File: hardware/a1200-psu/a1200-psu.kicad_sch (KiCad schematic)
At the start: 57 parts, among them J1 220V, J2 Conn_01x05, Q1 BC327, Q2 BC327, Q3 BU508AF, SW1 SW_SPST, U1 CNY17-2, U2 TL431D

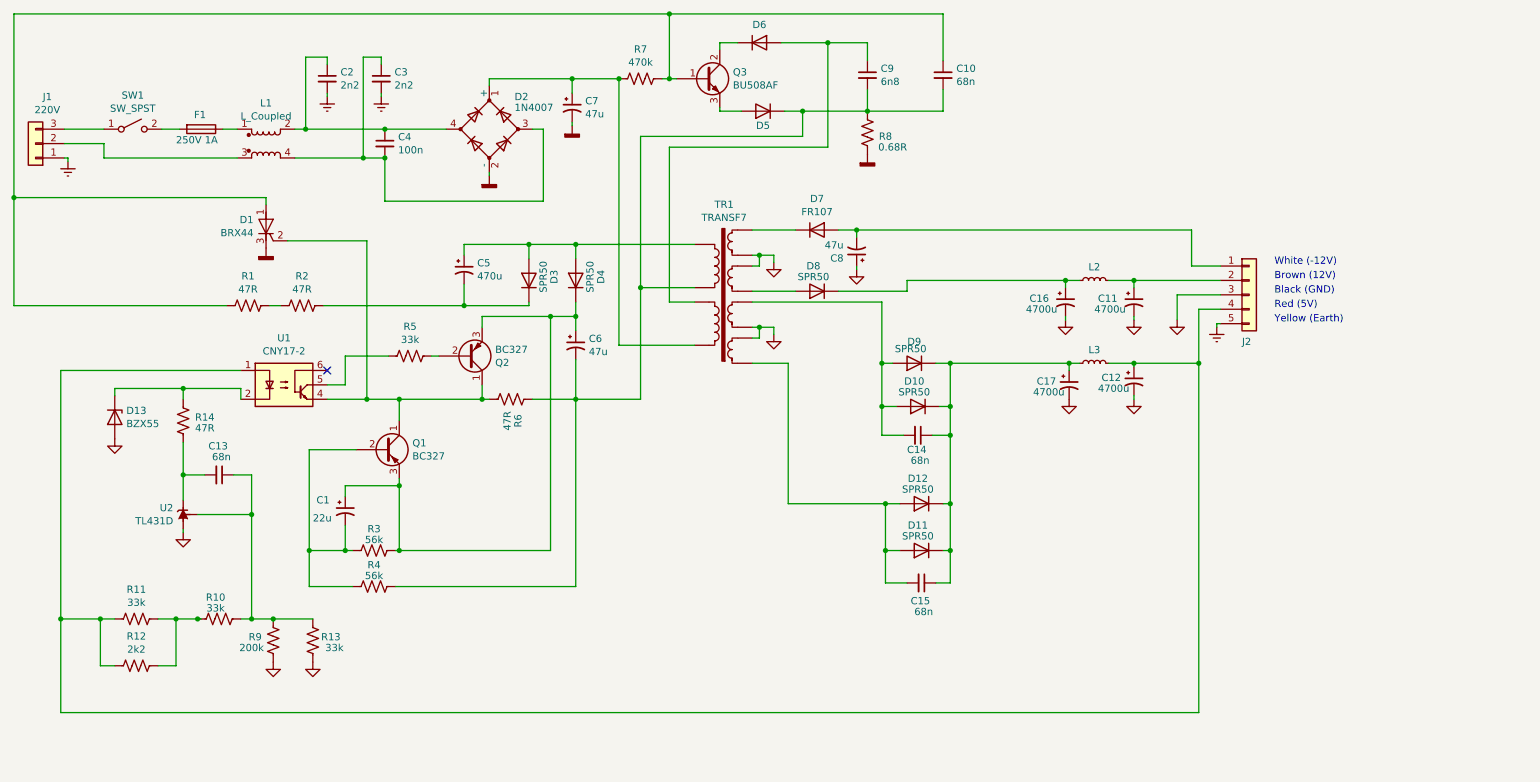
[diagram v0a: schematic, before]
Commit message: Add NTC and LF caps
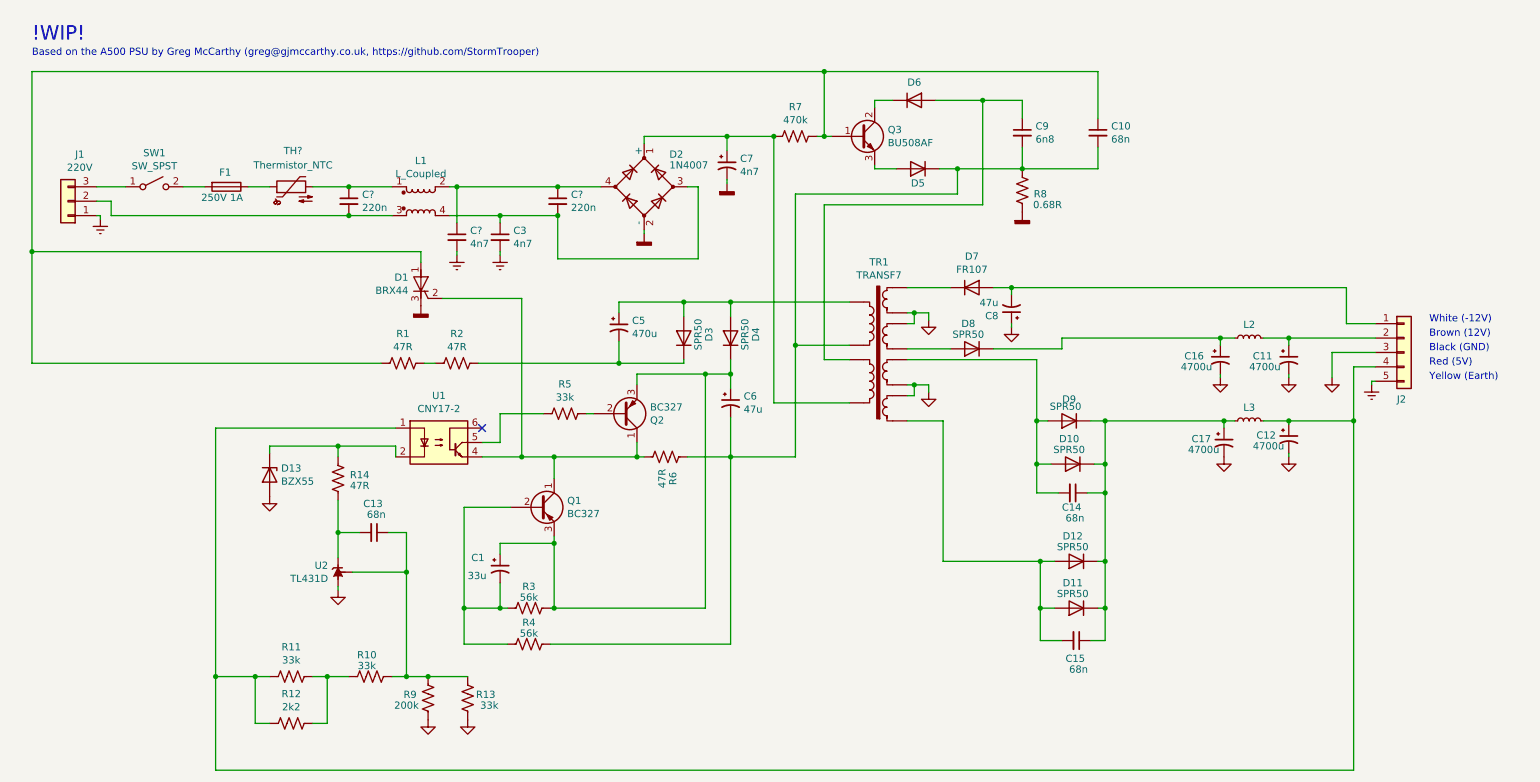
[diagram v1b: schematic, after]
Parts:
- removed C2: 2n2, symbol Device:C_Small
- removed C4: 100n, symbol Device:C_Small
- added C?: 4n7, symbol Device:C_Small
- added C? (x2): 220n, symbol Device:C_Small
- added TH?: Thermistor_NTC, symbol Device:Thermistor_NTC
- C1: value 22u -> 33u
- C3: value 2n2 -> 4n7
- C7: value 47u -> 4n7
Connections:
- net Earth: now also C?.2
- net at F1.1: now also TH?.1; no longer L1.1
- net at D2.4, L1.2: now also C?.1, C?.1
- net at J1.2 (Pin_2), L1.3: now also C?.2
- net at C3.1, D2.3, L1.4: now also C?.2
- new net: C?.1, L1.1, TH?.2
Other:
- note added: "!WIP!"
- note added: "Based on the A500 PSU by Greg McCarthy (greg@gjmccarthy.co.uk, https://github.com/StormTrooper)"
- company: (none) -> Nick Bolton
- title: Commodore A500 Power Supply  312503-03 -> Commodore A1200 Power Supply  391029-02
- moved on the sheet: C1, C10, C11, C12, C13, C14, C15, C16, C17, C3, C5, C6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

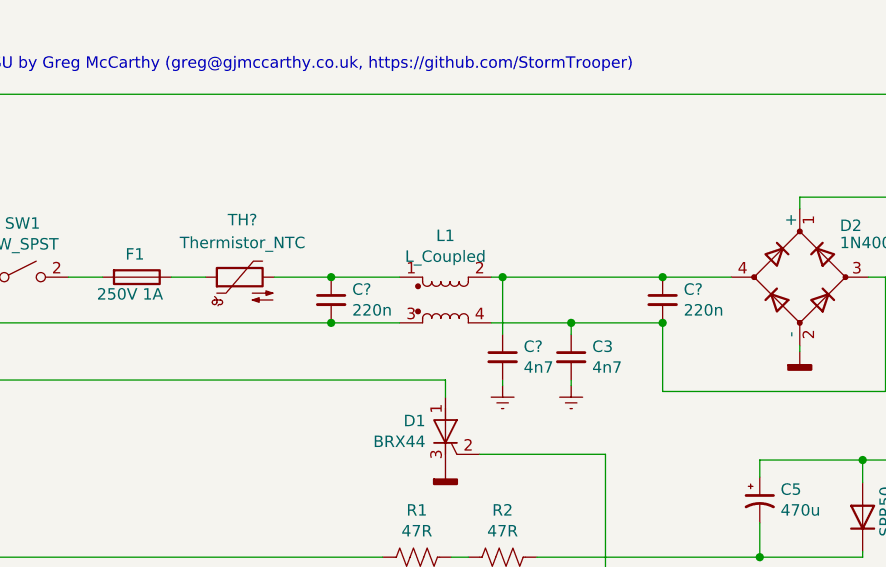
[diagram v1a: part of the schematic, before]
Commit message: Set TH value and annotate
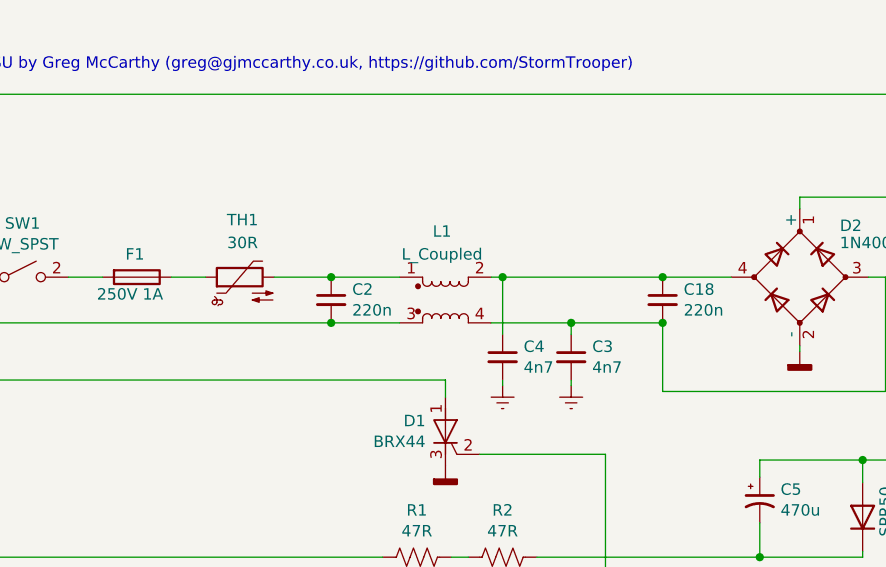
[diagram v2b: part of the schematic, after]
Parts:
- TH1: renamed from TH?; value Thermistor_NTC -> 30R
- gave numbers to parts that had none: 3
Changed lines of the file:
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@@
   )
   (symbol (lib_id "Device:L_Coupled") (at 87.63 46.99 0) (unit 1)
-    (in_bom yes) (on_board yes)
-    (property "Reference" "L1" (id 0) (at 87.63 39.8526 0))
-    (property "Value" "L_Coupled" (id 1) (at 87.63 42.164 0))
+    (in_bom yes) (on_board yes) (fields_autoplaced)
+    (property "Reference" "L1" (id 0) (at 87.249 39.37 0))
+    (property "Value" "L_Coupled" (id 1) (at 87.249 41.91 0))
     (property "Footprint" "" (id 2) (at 87.63 46.99 0)
       (effects (font (size 1.27 1.27)) hide)
@@
   (symbol (lib_id "Device:C_Small") (at 93.98 53.34 0) (unit 1)
     (in_bom yes) (on_board yes)
-    (property "Reference" "C?" (id 0) (at 96.3168 52.1716 0)
+    (property "Reference" "C4" (id 0) (at 96.3168 52.1716 0)
       (effects (font (size 1.27 1.27)) (justify left))
     )
@@
   (symbol (lib_id "power:Earth") (at 93.98 56.515 0) (unit 1)
     (in_bom yes) (on_board yes)
-    (property "Reference" "#PWR?" (id 0) (at 93.98 62.865 0)
+    (property "Reference" "#PWR03" (id 0) (at 93.98 62.865 0)
       (effects (font (size 1.27 1.27)) hide)
     )
@@
   (symbol (lib_id "Device:Thermistor_NTC") (at 64.77 44.45 90) (unit 1)
     (in_bom yes) (on_board yes) (fields_autoplaced)
-    (property "Reference" "TH?" (id 0) (at 65.0875 38.1 90))
-    (property "Value" "Thermistor_NTC" (id 1) (at 65.0875 40.64 90))
+    (property "Reference" "TH1" (id 0) (at 65.0875 38.1 90))
+    (property "Value" "30R" (id 1) (at 65.0875 40.64 90))
     (property "Footprint" "" (id 2) (at 63.5 44.45 0)
       (effects (font (size 1.27 1.27)) hide)
@@
   (symbol (lib_id "Device:C_Small") (at 111.76 46.99 0) (unit 1)
     (in_bom yes) (on_board yes)
-    (property "Reference" "C?" (id 0) (at 114.0968 45.8216 0)
+    (property "Reference" "C18" (id 0) (at 114.0968 45.8216 0)
       (effects (font (size 1.27 1.27)) (justify left))
     )
@@
   (symbol (lib_id "Device:C_Small") (at 74.93 46.99 0) (unit 1)
     (in_bom yes) (on_board yes)
-    (property "Reference" "C?" (id 0) (at 77.2668 45.8216 0)
+    (property "Reference" "C2" (id 0) (at 77.2668 45.8216 0)
       (effects (font (size 1.27 1.27)) (justify left))
     )
@@
       (reference "#PWR02") (unit 1) (value "GNDD") (footprint "")
     )
+    (path "/140d05a2-eaad-4824-bf22-b4c1b5fc3c05"
+      (reference "#PWR03") (unit 1) (value "Earth") (footprint "")
+    )
     (path "/00000000-0000-0000-0000-00005e6bda05"
       (reference "#PWR04") (unit 1) (value "Earth") (footprint "")
@@
       (reference "#PWR020") (unit 1) (value "GND") (footprint "")
     )
-    (path "/140d05a2-eaad-4824-bf22-b4c1b5fc3c05"
-      (reference "#PWR?") (unit 1) (value "Earth") (footprint "")
-    )
     (path "/00000000-0000-0000-0000-00005e80fecf"
       (reference "C1") (unit 1) (value "33u") (footprint "")
     )
+    (path "/9bd3b76d-6431-4e72-98c0-8c8f9369d359"
+      (reference "C2") (unit 1) (value "220n") (footprint "")
+    )
     (path "/00000000-0000-0000-0000-00005e6976c3"
       (reference "C3") (unit 1) (value "4n7") (footprint "")
     )
+    (path "/0e475606-0972-410d-9d2a-e185de5dfec3"
+      (reference "C4") (unit 1) (value "4n7") (footprint "")
+    )
     (path "/00000000-0000-0000-0000-00005e74c909"
       (reference "C5") (unit 1) (value "470u") (footprint "")
@@
       (reference "C17") (unit 1) (value "4700u") (footprint "")
     )
-    (path "/0e475606-0972-410d-9d2a-e185de5dfec3"
-      (reference "C?") (unit 1) (value "4n7") (footprint "")
-    )
     (path "/57508837-9844-4605-9233-1414d37064cf"
-      (reference "C?") (unit 1) (value "220n") (footprint "")
-    )
-    (path "/9bd3b76d-6431-4e72-98c0-8c8f9369d359"
-      (reference "C?") (unit 1) (value "220n") (footprint "")
+      (reference "C18") (unit 1) (value "220n") (footprint "")
     )
     (path "/00000000-0000-0000-0000-00005e6b8e8b"
@@
     )
     (path "/2facb6fc-ac96-441e-9800-d8af24285397"
-      (reference "TH?") (unit 1) (value "Thermistor_NTC") (footprint "")
+      (reference "TH1") (unit 1) (value "30R") (footprint "")
     )
     (path "/00000000-0000-0000-0000-00005e6e99dc"

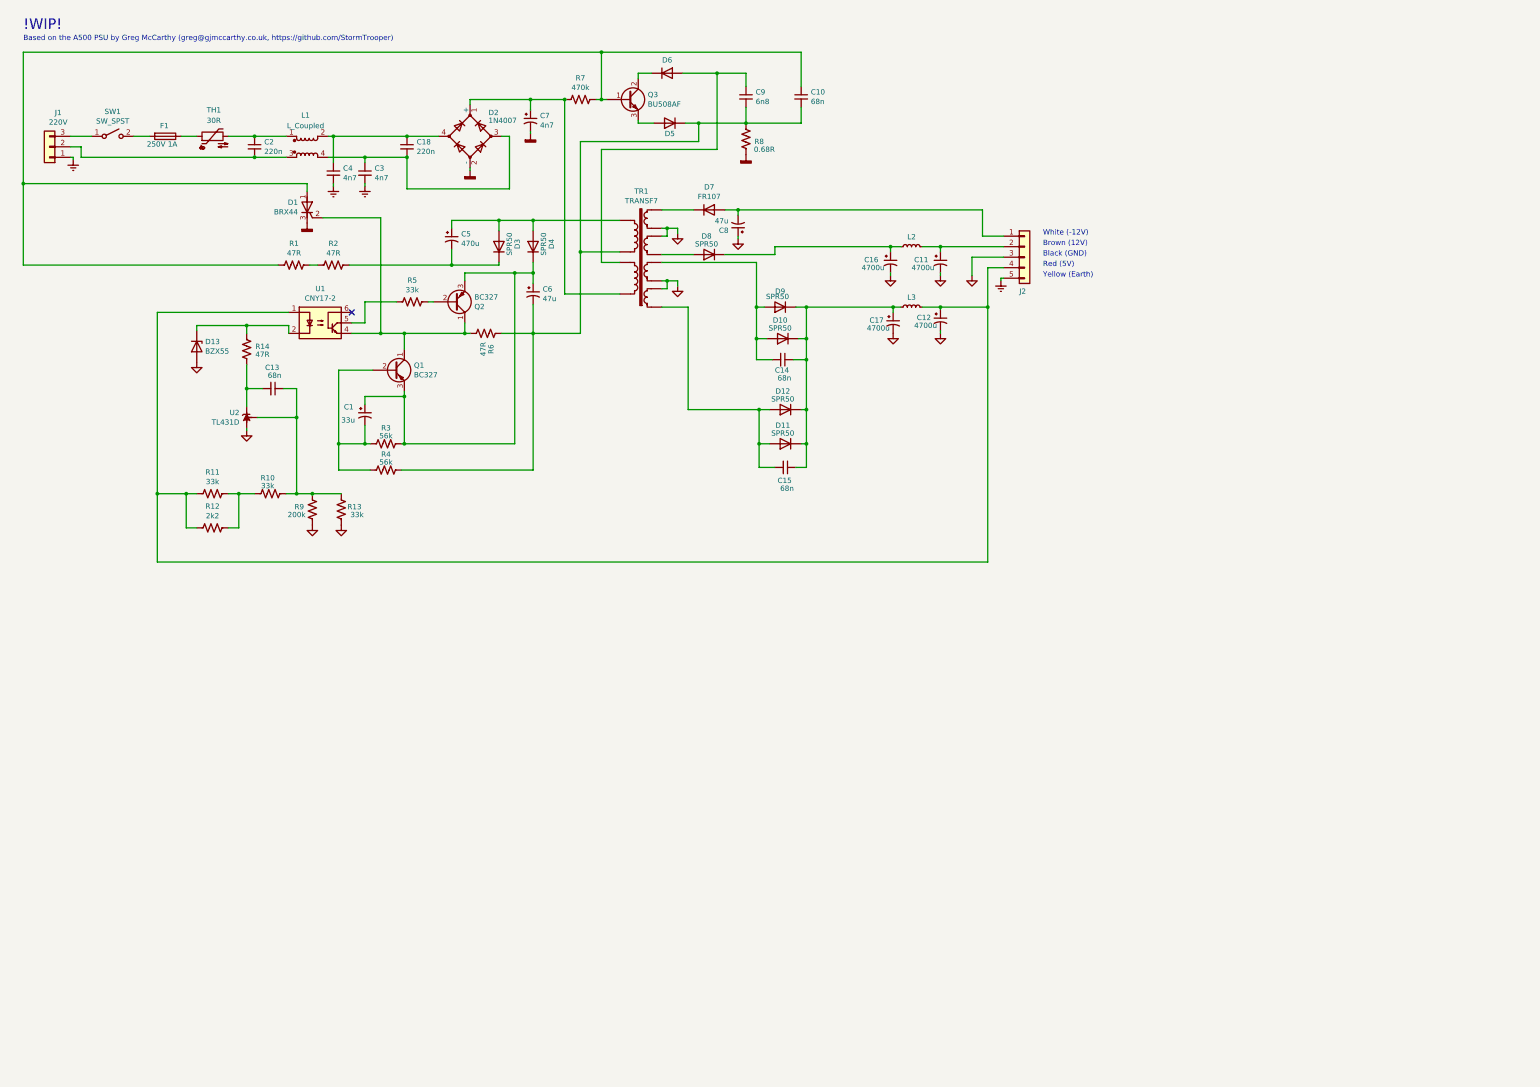
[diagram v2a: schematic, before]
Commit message: Matched transformer to A1200
Also:
- Segmented board into line/low
- Removed A500 diodes on 5V
- Added some TODOs
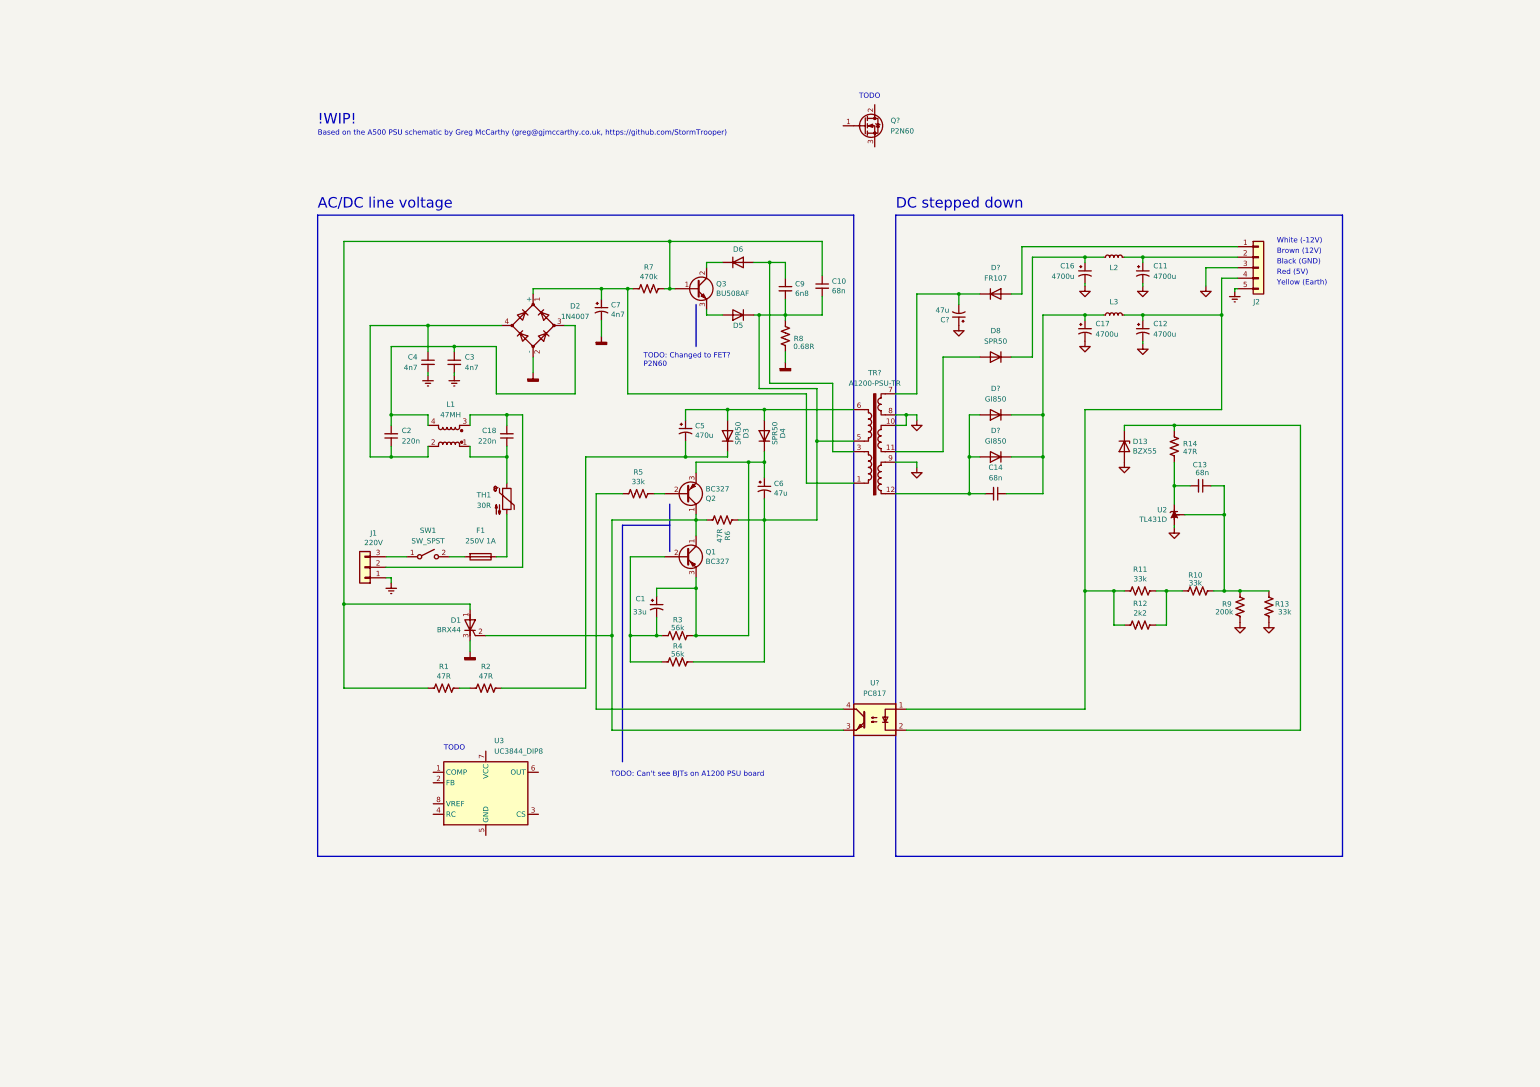
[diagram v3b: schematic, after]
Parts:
- removed C15: 68n, symbol Device:C_Small
- removed C8: 47u, symbol a500-psu-rescue:CP1_Small-Device
- removed D10, D11, D12, D9: SPR50, symbol Device:D
- removed D7: FR107, symbol Device:D
- removed TR1: TRANSF7, symbol transformer:TRANSF7
- removed U1: CNY17-2, symbol Isolator:CNY17-2
- added C?: 47u, symbol a500-psu-rescue:CP1_Small-Device
- added D?: FR107, symbol Device:D
- added D? (x2): GI850, symbol Device:D
- added Q?: P2N60, Package_TO_SOT_THT:TO-220-3_Vertical, symbol Device:Q_NMOS_GDS
- added TR?: A1200-PSU-TR, symbol Amiga A1200:A1200-PSU-TR
- added U3: UC3844_DIP8, Package_DIP:DIP-8_W7.62mm, symbol Regulator_Controller:UC3844_DIP8
- added U?: PC817, Package_DIP:DIP-4_W7.62mm, symbol Isolator:PC817
- L1: value L_Coupled -> 47MH
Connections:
- net GND: now also C?.1, TR?.10, TR?.8, TR?.9
- net at TH1.1: now also C18.1, L1.1; no longer F1.1
- net at C4.1, D2.4, L1.2: now also C2.1; no longer C18.1
- net at J1.2 (Pin_2), L1.3: now also C18.2; no longer C2.2
- net at C3.1, D2.3, L1.4: now also C2.2; no longer C18.2
- net at C12.1, J2.4 (Pin_4), L3.2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: now also U?.1
- net at D13.1 (K), R14.2: now also U?.2
- net at D1.2 (G), Q1.1 (C), Q2.1 (C)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: now also U?.3
- net at R5.2: now also U?.4
- net at C9.1, D6.2 (A): now also TR?.3
- net at C7.1, D2.1 (+), R7.2: now also TR?.1
- net at C10.2, C6.2, C9.2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: now also TR?.5
- net at C5.1, D3.2 (A), D4.2 (A): now also TR?.6
- net at C14.2: now also D?.2 (A), D?.2 (A), TR?.12
- net at D8.2 (A): now also TR?.11
- net at J2.1 (Pin_1): now also D?.2 (A)
- net at C14.1, C17.1, L3.1: now also D?.1 (K), D?.1 (K)
- new net: C?.2, D?.1 (K), TR?.7
- new net: F1.1, TH1.2
- no-connect marks 1 -> 0
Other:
- note added: "AC/DC line voltage"
- note added: "Based on the A500 PSU schematic by Greg McCarthy (greg@gjmccarthy.co.uk, https://github.com/StormTrooper)"
- note added: "DC stepped down"
- note added: "TODO"
- note added: "TODO: Can't see BJTs on A1200 PSU board"
- note added: "TODO: Changed to FET? P2N60"
- note removed: "Based on the A500 PSU by Greg McCarthy (greg@gjmccarthy.co.uk, https://github.com/StormTrooper)"
- moved on the sheet: C1, C10, C11, C12, C13, C14, C16, C17, C3, C4, C5, C6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
